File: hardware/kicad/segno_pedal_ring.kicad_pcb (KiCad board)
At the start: 2 copper layers, 68 x 68 mm, 11 parts, among them J1 JST-XH 8P, J2 NEOPIXEL, J3 RINGPINS24

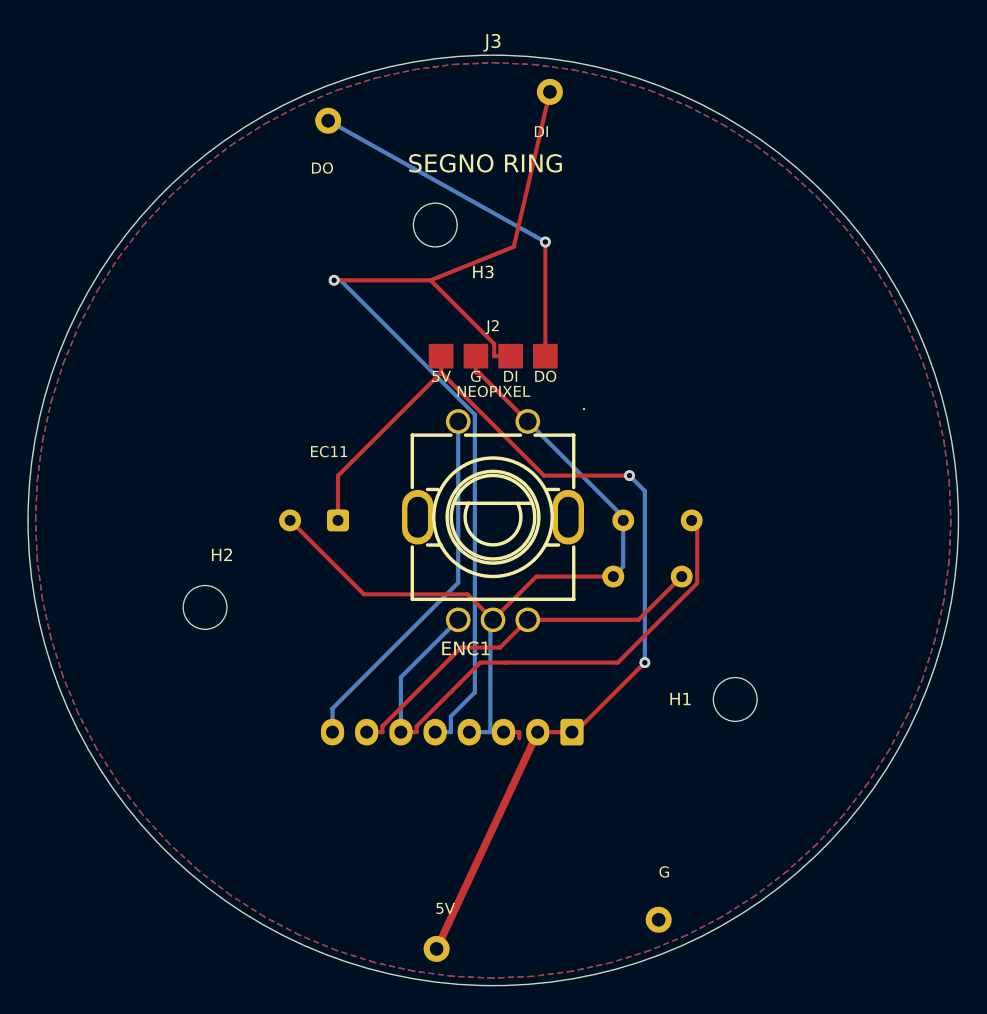
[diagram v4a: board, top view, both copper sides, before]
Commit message: refactor(hardware): autoroute the ring board, then put the power width back
Full rip-up and Freerouting pass over segno_pedal_ring, as asked. 68 tracks and
vias out, DSN -> Freerouting 1.9.0 -> SES back in, zones refilled.

Result: 41 tracks, ZERO vias, and GND carried entirely by the pour -- tidier than
the hand-routed version, which needed a via for RING_DOUT to dodge RING_DATA and
another to restore a layer transition. The autorouter found a single-layer
solution for every signal.

BUT IT SIZED THE POWER NET LIKE A SIGNAL. Every trace came back 0.30 mm, +5V_LED
included. That net carries ~1.44 A with 24 WS2812Bs at full white; IPC-2221 for a
10 C rise on 1 oz external copper wants 0.50 mm, so 0.30 would have run hot. This
is the exact failure the pcb-layout skill warns about -- 'autorouter-chosen trace
widths' -- and it is invisible to DRC, which passed 0/0 on the undersized board.

Widened +5V_LED back out, taking the widest that still passes: 0.80 and 0.65 each
leave one clearance violation, 0.55 is clean and sits above the 0.50 minimum.
Recorded here because the margin is thin: if this board is ever re-routed, the
power width has to be re-applied afterwards, and 0.55 is the ceiling, not a
preference.

Freerouting 2.3.0 needs Java 25 and this machine has 17; 1.9.0 (the version the
skill names) runs fine.

Verified after routing: DRC 0 violations / 0 unconnected; the four Ring 24 pads
still match Adafruit's board file to 0.0006 mm; board still O68.00. Gerbers
re-exported; the phantom .kicad_pro top_level_sheets block reverted again.
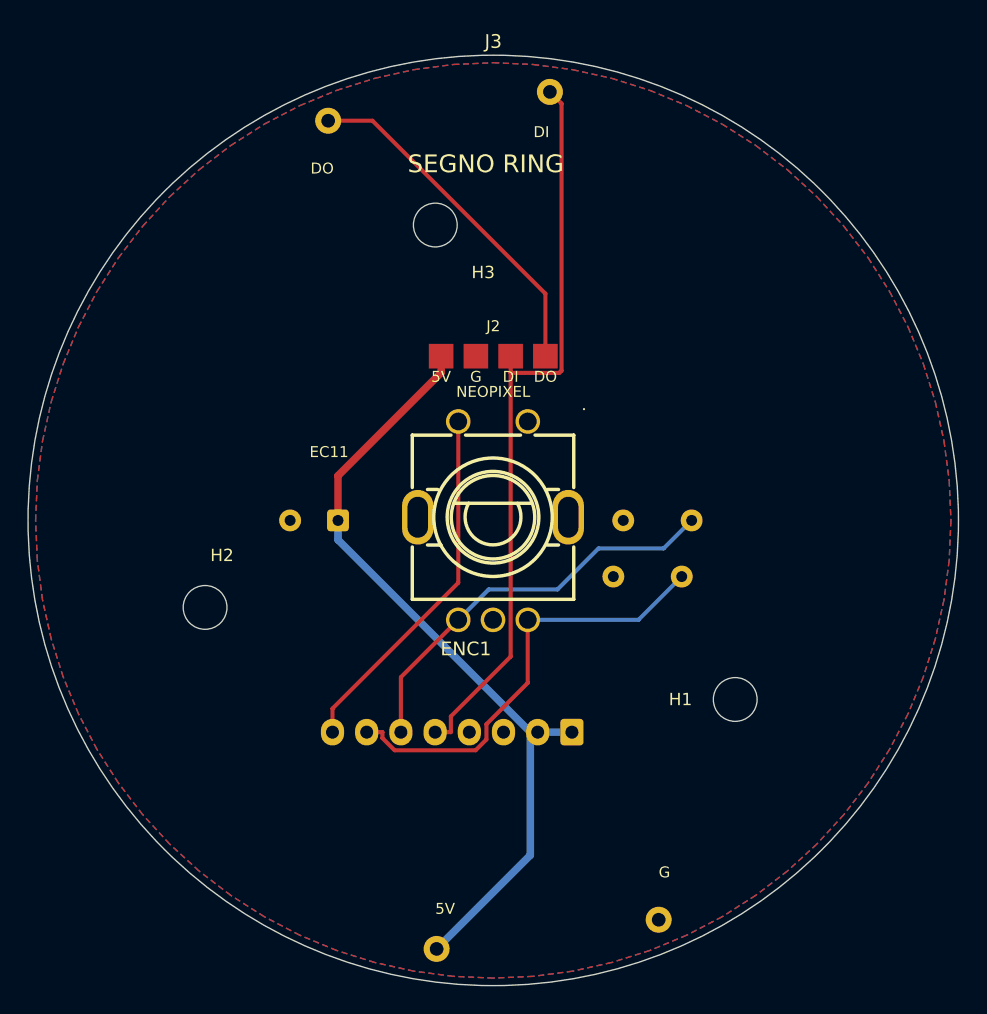
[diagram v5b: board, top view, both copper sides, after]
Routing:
- net GND: track 61.3 -> 0.00 mm
- net RING_DATA: track 73.3 -> 54.9 mm, vias 1 -> 0
- net +5V_LED: track 73.6 -> 58.1 mm, vias 2 -> 0
- net ENC_A: track 41.1 -> 30.0 mm
- net ENC_B: track 28.0 -> 32.4 mm
- net RING_DOUT: track 26.5 -> 25.7 mm, vias 1 -> 0
